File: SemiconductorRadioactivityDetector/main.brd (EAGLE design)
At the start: 32 parts, among them IC1 317T, IC3 LM324N, Q1 2N4093

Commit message: PCB done.
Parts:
- removed C11: 100n, resistor:C1206
- removed IC3: LM324N, linear:DIL14
- removed INTEGRATED_OUTPUT, LOGIC_LEVEL_OUTPUT, RAW_OUTPUT1: 22-05-7028-02, con-molex:7395-02
- removed R16: 10M, resistor:0204V
- added C10: 100n, resistor:C1206
- added IC2: 317T, linear:TO220H
- added J2, J3, J4: 22-23-2021, con-molex:22-23-2021
- added R8: 240R, resistor:M1206
- C1: value 15n -> 100n
- C6: value 100n -> 15n
- IC1: value 317T -> LM324N; device linear:TO220H -> linear:DIL14
- R1: value 240R -> 10M; device resistor:M1206 -> resistor:0204V
- R10: value 1M -> 4k7
- R11: value 100k -> 1k; device resistor:M1206 -> pot:B64Y
- R12: device resistor:M1206 -> resistor:R1206
- R13: value 1M -> 100k
- R14: value 47k -> 1M
- R2: value 2k -> 1M
- R3: value 1M -> 47k
- R5: value 100k -> 1M
- R7: value 1k -> 100k; device pot:B64Y -> resistor:M1206
- R9: value 4k7 -> 2k
- moved Q1 237.3 mm to (67.3, 14.0), flipped to the bottom
- moved D1 236.8 mm to (72.4, 15.2), flipped to the bottom
- moved C9 221.4 mm to (32.4, 6.35), flipped to the bottom, turned to 270 degrees
- moved R14 188.8 mm to (29.2, 6.35), flipped to the bottom, turned to 90 degrees
- moved C8 188.6 mm to (13.3, 10.2), flipped to the bottom
- moved R13 185.1 mm to (32.4, 12.1), flipped to the bottom, turned to 90 degrees
- moved C5 184.6 mm to (19.1, 14.6), flipped to the bottom, turned to 90 degrees
- moved C6 159.6 mm to (58.4, 19.1), flipped to the bottom, turned to 90 degrees
- moved R12 157.6 mm to (35.6, 12.1), flipped to the bottom, turned to 270 degrees
- moved R11 153.9 mm to (28.6, 17.8), turned to 90 degrees
- moved R10 141.7 mm to (25.4, 12.1), flipped to the bottom, turned to 90 degrees
- moved R7 133.3 mm to (50.2, 19.1), flipped to the bottom, turned to 270 degrees
- moved R6 126.4 mm to (54.6, 17.1), flipped to the bottom
- moved C1 121.7 mm to (71.1, 10.2), flipped to the bottom
- moved R9 112.5 mm to (10.8, 5.71), flipped to the bottom, turned to 270 degrees
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- renumbered POWER_SUPPLY to J1
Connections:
- net GND: now also C6.2, IC1.11, J2.2, J3.2, J4.1, R1.2, R11.A, R9.1; no longer C11.2, IC3.11, INTEGRATED_OUTPUT.2, LOGIC_LEVEL_OUTPUT.1, R16.2, R2.1, R7.A, RAW_OUTPUT1.2
- net N$1: now also IC2.1, R8.1, R9.2; no longer IC1.1, R1.1, R2.2
- net N$11: now also IC1.9, R11.S; no longer IC3.9, R7.S
- net N$12: now also C10.1, IC1.13, R13.1, R14.2; no longer C6.1, IC3.13, R10.2, R11.1
- net N$13: now also C10.2, IC1.14, J3.1, R14.1; no longer C6.2, IC3.14, INTEGRATED_OUTPUT.1, R10.1
- net N$14: now also IC1.12; no longer IC3.12
- net N$15: now also IC1.8, J4.2; no longer IC3.8, LOGIC_LEVEL_OUTPUT.2
- net N$16: now also C1.1, R2.2; no longer C5.1, R13.2
- net N$17: now also R1.1; no longer R16.1
- net N$18: now also IC1.3, R3.1; no longer IC3.3, R14.1
- net N$19: now also IC1.10, IC1.7, J2.1, R13.2, R7.1; no longer IC3.10, IC3.7, R11.2, R5.1, RAW_OUTPUT1.1
- net N$2: now also IC1.2, R5.2; no longer IC3.2, R3.2
- net N$3: now also IC1.1, IC1.5, R5.1; no longer IC3.1, IC3.5, R3.1
- net N$4: now also C4.1; no longer C1.1
- net N$5: now also IC1.6, R7.2; no longer IC3.6, R5.2
- net N$7: now also C6.1; no longer C4.1
- net N$8: now also C5.1, IC2.3; no longer C2.1, IC1.3
- net N$9: now also R10.2, R11.E; no longer R7.E, R9.2
- net VCC: now also C2.1, IC1.4, IC2.2, R10.1, R2.1, R3.2, R8.2; no longer C11.1, IC1.2, IC3.4, R1.2, R13.1, R14.2, R9.1
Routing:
- net VCC: track 8.44 -> 94.1 mm
- net N$19: track 0.00 -> 26.7 mm
- net N$18: track 0.00 -> 23.8 mm
- net N$3: track 0.00 -> 17.7 mm, vias 0 -> 2
- net N$13: track 0.00 -> 13.4 mm
- net N$12: track 0.00 -> 12.5 mm
- net N$11: track 0.00 -> 10.2 mm
- net N$17: track 0.00 -> 9.79 mm
- net N$5: track 0.00 -> 7.12 mm
- net N$2: track 0.00 -> 6.40 mm
- net N$16: track 0.00 -> 5.77 mm
- net N$9: track 0.00 -> 4.21 mm
- net N$15: track 0.00 -> 4.07 mm
- net N$14: track 0.00 -> 3.38 mm
- net N$4: track 0.00 -> 3.18 mm
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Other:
- board text added: "OUT INTEG."
- board text added: "OUT LOGIC."
- board text added: "OUT RAW"
- board text added: "POWER SUPPLY 14-16V DC"
- board text removed: "DC IN SUPPLY"
- board text removed: "HIGH VOLTAGE"
- board text removed: "HV OUT A"
- board text removed: "HV OUT B"

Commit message: Second version. Not working.
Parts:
- removed J2, J3, J4: 22-23-2021, con-molex:22-23-2021
- removed R14: 1M, resistor:M1206
- added C11: 10n, resistor:C0805
- added C12: 10n, rcl:C0805
- added C13: 100n, rcl:C0805
- added C14, C15: 100p, resistor:C0805
- added C16: 100n, resistor:C0805
- added IC3: OPA2333D, linear:SO08
- added PAD1, PAD2: (no value), wirepad:1,6/0,8
- added TP1, TP2, TP3, TP5: PTR1TP12R, testpad:TP12R
- C1, C5, C8: device resistor:C1206 -> rcl:C0805
- C10: value 100n -> 4p7; device resistor:C1206 -> resistor:C0805
- C2: value 100n -> 330n; device resistor:C1206 -> rcl:C0805
- C4: value 15n -> 330n; device resistor:C1206 -> rcl:C0805
- C6: value 15n -> 10n; device resistor:C1206 -> resistor:C0805
- C7: value 100n -> 10n; device resistor:C1206 -> resistor:C0805
- C9: value 100n -> 100p; device resistor:C1206 -> resistor:C0805
- IC1: value LM324N -> 78L08Z; device linear:DIL14 -> linear:TO92
- IC2: value 317T -> OPA2333D; device linear:TO220H -> linear:SO08
- R10: value 4k7 -> 1k; device resistor:M1206 -> rcl:R0805
- R11: device pot:B64Y -> rcl:R0805
- R12: value 100k -> 10k; device resistor:R1206 -> rcl:R0805
- R13: value 100k -> 10k; device resistor:M1206 -> rcl:R0805
- R2: value 1M -> 10k; device resistor:M1206 -> rcl:R0805
- R3: value 47k -> 10k; device resistor:M1206 -> rcl:R0805
- R4: value 1k -> 470k; device resistor:M1206 -> rcl:R0805
- R5: value 1M -> 39k; device resistor:M1206 -> rcl:R0805
- R6: value 1k -> 10R; device resistor:M1206 -> rcl:R0805
- R7: value 100k -> 1k; device resistor:M1206 -> rcl:R0805
- R8: value 240R -> 10k; device resistor:M1206 -> rcl:R0805
- R9: value 2k -> 10M; device resistor:M1206 -> rcl:0204V
- moved R2 68.9 mm to (5.08, 26.7)
- moved C1 68.9 mm to (3.17, 21.6)
- moved R3 63.0 mm to (5.08, 24.1), turned to 0 degrees
- moved C7 47.7 mm to (3.17, 10.2), turned to 90 degrees
- moved R7 45.0 mm to (5.71, 12.1)
- moved Q1 41.5 mm to (26.0, 10.2)
- moved D1 41.4 mm to (31.1, 12.1)
- moved R6 38.4 mm to (17.8, 6.35), turned to 180 degrees
- moved R1 38.3 mm to (26.7, 14.6)
- moved C6 38.0 mm to (21.6, 9.53), turned to 0 degrees
- moved C4 33.7 mm to (22.2, 5.71)
- moved C2 32.4 mm to (30.5, 6.99), turned to 0 degrees
- moved C9 31.4 mm to (3.17, 17.8)
- moved IC1 30.5 mm to (14.0, 23.5), turned to 0 degrees
- moved R13 29.9 mm to (3.17, 5.71), turned to 270 degrees
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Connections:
- removed net N$1: IC2.1, R8.1, R9.2
- removed net N$12: C10.1, C9.1, IC1.13, R13.1, R14.2
- removed net N$18: IC1.3, Q1.2, R3.1
- removed net N$19: IC1.10, IC1.7, J2.1, R13.2, R7.1
- removed net N$5: IC1.6, R6.2, R7.2
- removed net VCC: C2.1, C7.1, C8.1, IC1.4, IC2.2, R10.1, R2.1, R3.2, R8.2
- new net N$10: C9.1, IC2.2, R7.1, R8.2
- new net N$20: C10.2, C11.1, IC3.1, R9.1
- new net N$22: C12.1, C9.2, IC2.1, R8.1
- new net N$6: C6.1, Q1.2, R5.1
- new net V+: C13.1, C16.1, C4.1, C8.1, IC1.1, IC2.8, IC3.8, R2.2, R4.1, R5.2, TP3.TP
- new net V_REF: C1.1, IC2.3, IC2.5, IC3.3, IC3.5, R2.1, R3.2, TP1.TP
- net GND: now also C13.2, C16.2, IC1.2, IC2.4, IC3.4, PAD2.1, R3.1; no longer C6.2, C7.2, IC1.11, J2.2, J3.2, J4.1, R11.A, R12.1, R9.1
- net N$11: now also C7.2, R7.2; no longer IC1.9, R11.S
- net N$13: now also C14.1, IC2.6, R11.1, R12.2; no longer C10.2, C9.2, IC1.14, J3.1, R14.1
- net N$14: now also C12.2, R11.2; no longer IC1.12, R12.2
- net N$15: now also C11.2, R10.2; no longer IC1.8, J4.2
- net N$16: now also C2.1, R4.2; no longer C1.1, R2.2
- net N$2: now also C6.2, R6.2; no longer IC1.2, R4.2, R5.2
- net N$3: now also C14.2, IC2.7, PAD1.1, R12.1; no longer IC1.1, IC1.5, R5.1
- net N$4: now also C10.1, IC3.2, R6.1, R9.2; no longer C4.1, R4.1
- net N$7: now also C15.2, C7.1, IC3.7, R13.1, TP5.TP; no longer C6.1, R6.1
- net N$8: now also IC1.3, TP2.TP; no longer IC2.3
- net N$9: now also C15.1, IC3.6, R10.1, R13.2; no longer R10.2, R11.E
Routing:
- net VCC: track 94.1 -> 0.00 mm
- net V+: track 0.00 -> 76.5 mm, vias 0 -> 3
- net V_REF: track 0.00 -> 41.5 mm, vias 0 -> 2
- net N$19: track 26.7 -> 0.00 mm
- net N$18: track 23.8 -> 0.00 mm
- net N$10: track 0.00 -> 17.9 mm
- net N$12: track 12.5 -> 0.00 mm
- net N$22: track 0.00 -> 8.82 mm
- net N$1: track 8.31 -> 0.00 mm
- net N$9: track 4.21 -> 12.4 mm
- net N$7: track 2.73 -> 10.6 mm
- net N$11: track 10.2 -> 2.54 mm
- net N$20: track 0.00 -> 7.30 mm
- net N$3: track 17.7 -> 10.5 mm, vias 2 -> 0
- net N$5: track 7.12 -> 0.00 mm
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- added copper zone on layer 1, net GND
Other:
- board outline added: 34.9 x 32.4 mm
- board text added: "rev3.0"
- board text removed: "OUT INTEG."
- board text removed: "OUT LOGIC."
- board text removed: "OUT RAW"
- board text removed: "POWER SUPPLY 14-16V DC"
- board text removed: "rev2.0"

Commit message: Third HW revision, paritialy done.
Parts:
- removed C10: 4p7, resistor:C0805
- removed C11: 10n, resistor:C0805
- removed C12: 10n, rcl:C0805
- removed C13: 100n, rcl:C0805
- removed C14, C15, C9: 100p, resistor:C0805
- removed C16: 100n, resistor:C0805
- removed IC3: OPA2333D, linear:SO08
- removed J1: 22-05-7028-02, con-molex:7395-02
- removed PAD1, PAD2: (no value), wirepad:1,6/0,8
- removed Q1: 2N4093, transistor-fet:TO18
- removed R11: 1k, rcl:R0805
- removed R12, R13: 10k, rcl:R0805
- removed TP1, TP2, TP5: PTR1TP12R, testpad:TP12R
- added D2, D3: BPW32, opto-trans-siemens:BPW32
- added SL1: (no value), con-amp-quick:02P
- added U1: TPS7A470, regulator-jqi:S-PVQFN-N20
- added X1: LTI-SASF54GT, con-coax:LTI-SASF54GT
- C1, C5: value 100n -> 330n
- C2: value 330n -> (none); device rcl:C0805 -> resistor:T/3528-12R
- C3: value 100u/16V -> 100n; device rcl:153CLV-0505 -> rcl:C0805
- C6: value 10n -> 100n; device resistor:C0805 -> rcl:C0805
- C7: value 10n -> 330n; device resistor:C0805 -> rcl:C0805
- C8: value 100n -> 330n; device rcl:C0805 -> rcl:C1206K
- D1: value BP104 -> BPW32; device opto-trans-siemens:BP104 -> opto-trans-siemens:BPW32
- IC1: value 78L08Z -> LF356D; device linear:TO92 -> linear:SO08
- IC2: value OPA2333D -> LF356D
- R1: value 10M -> 10k; device resistor:0204V -> rcl:R1206
- R10, R7: value 1k -> 10k
- R3: value 10k -> (none); device rcl:R0805 -> resistor:MINI_MELF-0204W
- R4: value 470k -> (none); device rcl:R0805 -> resistor:MINI_MELF-0204W
- R5: value 39k -> (none); device rcl:R0805 -> resistor:RTRIM64W
- R6: value 10R -> (none); device rcl:R0805 -> resistor:M0805
- R8: value 10k -> (none); device rcl:R0805 -> resistor:M0805
- R9: value 10M -> (none); device rcl:0204V -> resistor:M0805
- moved R8 27.3 mm to (29.0, 3.57), turned to 180 degrees
- moved C7 25.6 mm to (28.8, 10.7), turned to 180 degrees
- moved D1 25.5 mm to (5.59, 11.2), flipped to the top, turned to 90 degrees
- moved R3 21.7 mm to (12.7, 3.81), turned to 270 degrees
- moved IC2 21.5 mm to (28.2, 7.11)
- moved C6 19.9 mm to (24.8, 29.2), turned to 180 degrees
- moved C8 19.3 mm to (19.2, 7.75), turned to 180 degrees
- moved R5 19.1 mm to (5.75, 4.00), turned to 180 degrees
- moved R7 18.7 mm to (24.4, 10.8), turned to 180 degrees
- moved TP3 18.2 mm to (22.2, 17.8)
- moved C5 17.1 mm to (14.0, 7.62)
- moved C2 17.1 mm to (29.3, 24.0), turned to 90 degrees
- moved R9 16.6 mm to (33.6, 9.06), flipped to the bottom, turned to 90 degrees
- moved R4 15.3 mm to (15.2, 3.81), turned to 90 degrees
- moved R10 12.5 mm to (22.9, 6.86)
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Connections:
- removed net N$11: C7.2, R7.2
- removed net N$13: C14.1, IC2.6, R11.1, R12.2
- removed net N$16: C2.1, D1.K, R4.2
- removed net N$17: D1.A, Q1.3, R1.1
- removed net N$20: C10.2, C11.1, IC3.1, R9.1
- removed net N$22: C12.1, C9.2, IC2.1, R8.1
- removed net V_REF: C1.1, IC2.3, IC2.5, IC3.3, IC3.5, R2.1, R3.2, TP1.TP
- new net N$1: C5.2, C8.1, IC1.6, R4.2
- new net N$5: C6.1, U1.14
- net GND: now also C2.-, C3.2, C6.2, C7.2, D1.A, D2.A, D3.A, IC1.4, R10.1, R2.1, R6.1, SL1.1, U1.10, U1.11, U1.12, U1.17, U1.18, U1.19, U1.2, U1.4, U1.5, U1.6, U1.7, U1.8, U1.9, U1.EXP, X1.2, X1.3, X1.4, X1.5; no longer C13.2, C16.2, C2.2, C3.-, C5.2, C8.2, IC1.2, IC3.4, J1.2, PAD2.1, Q1.1, R1.2, R3.1
- net N$10: now also C8.2, IC2.3, R10.2; no longer C9.1, IC2.2, R8.2
- net N$14: now also C1.1, IC1.3, R1.1, R2.2; no longer C12.2, R11.2
- net N$15: now also R9.2, X1.1; no longer C11.2, R10.2
- net N$2: now also IC2.2, R8.1; no longer C6.2
- net N$3: now also R3.2, R4.1; no longer C14.2, IC2.7, PAD1.1, R12.1
- net N$4: now also C5.1, D1.K, D2.K, D3.K, IC1.2, R3.1; no longer C10.1, IC3.2, R6.1, R9.2
- net N$6: now also IC1.1; no longer C6.1, Q1.2
- net N$7: now also IC1.5, R5.3; no longer C15.2, C7.1, IC3.7, R13.1, TP5.TP
- net N$8: now also C2.+, C3.1, SL1.2, U1.13, U1.15, U1.16; no longer C3.+, C5.1, IC1.3, J1.1, TP2.TP
- net N$9: now also IC2.6, R8.2, R9.1; no longer C15.1, IC3.6, R10.1, R13.2
- net V+: now also C7.1, IC1.7, IC2.7, R1.2, R7.2, U1.1, U1.20, U1.3; no longer C13.1, C16.1, C8.1, IC1.1, IC2.8, IC3.8, R2.2, R4.1
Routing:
- net V_REF: track 41.5 -> 0.00 mm, vias 2 -> 0
- net N$7: track 10.6 -> 27.7 mm, vias 0 -> 2
- net V+: track 76.5 -> 63.5 mm, vias 3 -> 0
- net N$13: track 11.8 -> 0.00 mm
- net N$1: track 0.00 -> 11.6 mm
- net N$10: track 17.9 -> 8.19 mm
- net N$22: track 8.82 -> 0.00 mm
- net N$14: track 2.54 -> 11.2 mm
- net N$15: track 2.54 -> 10.8 mm
- net N$17: track 8.04 -> 0.00 mm
- net N$3: track 10.5 -> 2.54 mm
- net N$4: track 9.06 -> 17.0 mm
- net N$20: track 7.30 -> 0.00 mm
- net N$8: track 12.6 -> 17.9 mm, vias 0 -> 2
- net N$16: track 5.21 -> 0.00 mm
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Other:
- board text added: "rev4.0"
- board text removed: "rev3.0"

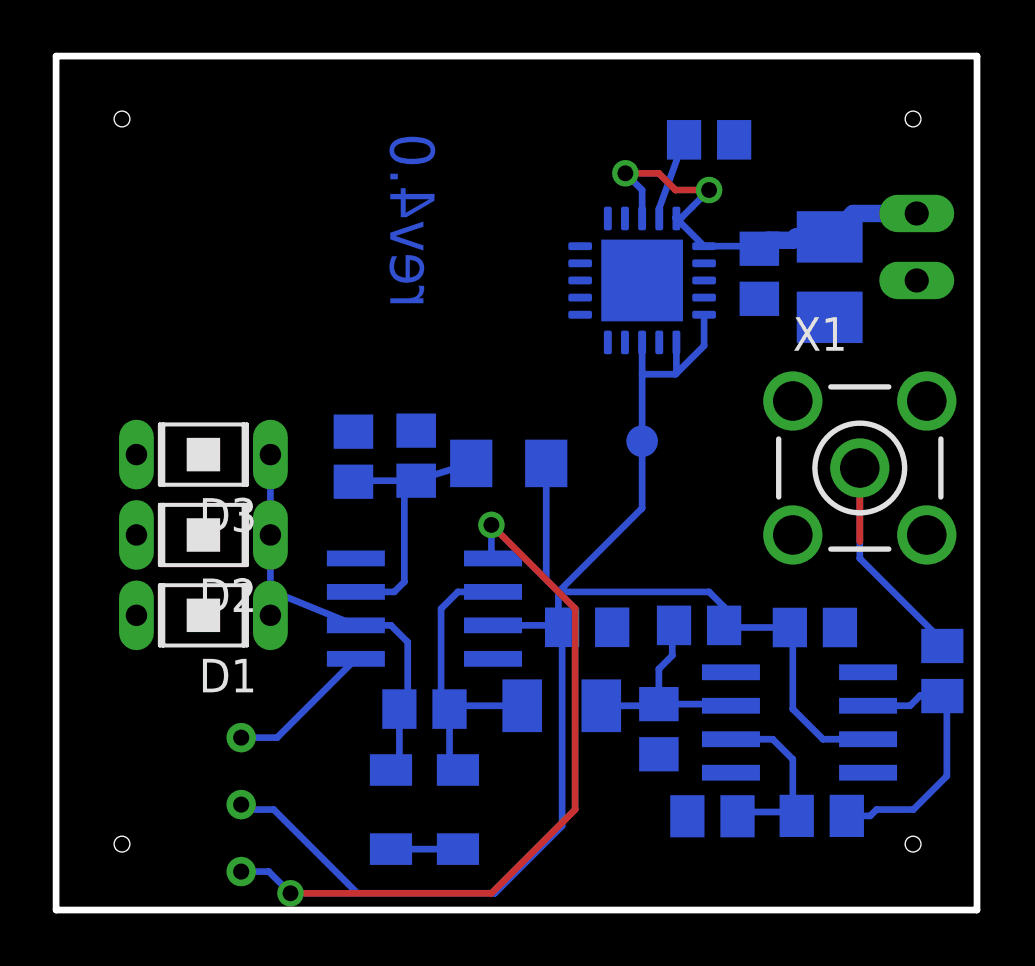
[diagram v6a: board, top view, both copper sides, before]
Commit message: Removed obsolete project, PCB fixes.
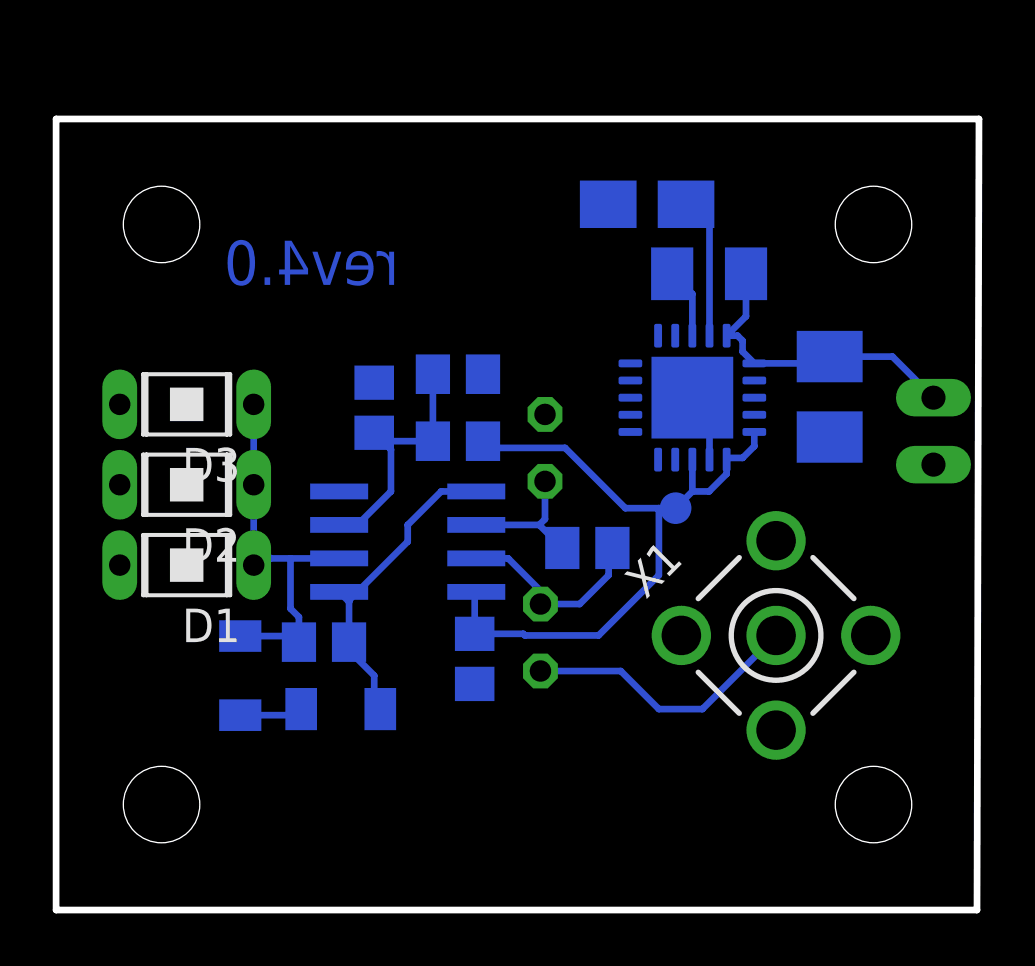
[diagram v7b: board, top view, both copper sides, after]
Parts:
- removed C4, C7: 330n, rcl:C0805
- removed C8: 330n, rcl:C1206K
- removed IC1, IC2: LF356D, linear:SO08
- removed R10, R7: 10k, rcl:R0805
- added IC3: NE5532D, linear:SO08
- C6: device rcl:C0805 -> rcl:A/3216-18W
- R1: device rcl:R1206 -> rcl:R0805
- R5: device resistor:RTRIM64W -> resistor:M1206
- R6, R9: device resistor:M0805 -> resistor:0204V
- moved R5 27.7 mm to (24.8, 24.1), turned to 0 degrees
- moved C3 18.2 mm to (15.9, 9.53)
- moved R6 15.3 mm to (18.5, 17.5), turned to 270 degrees
- moved R9 15.3 mm to (18.4, 10.3), turned to 270 degrees
- moved R8 13.5 mm to (20.1, 13.7)
- moved R3 7.65 mm to (6.99, 8.89)
- moved X1 7.10 mm to (27.3, 10.4), turned to 45 degrees
- moved SL1 7.01 mm to (33.3, 18.2)
- moved R4 5.85 mm to (10.8, 7.62), turned to 180 degrees
- moved R2 5.05 mm to (15.2, 20.3), turned to 0 degrees
- moved U1 4.84 mm to (24.1, 19.4)
- moved C5 4.58 mm to (10.2, 10.2)
- moved C2 4.54 mm to (29.3, 19.5)
- moved C6 3.39 mm to (22.4, 26.8)
- moved TP3 2.84 mm to (23.5, 15.2)
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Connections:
- removed net N$10: C8.2, IC2.3, R10.2, R7.1
- removed net N$7: IC1.5, R5.3
- net GND: now also C6.-, IC3.4; no longer C4.2, C6.2, C7.2, IC1.4, IC2.4, R10.1, U1.12, U1.6, U1.9
- net N$1: now also IC3.1, IC3.5; no longer C8.1, IC1.6
- net N$14: now also IC3.3; no longer IC1.3
- net N$2: now also IC3.6; no longer IC2.2
- net N$4: now also IC3.2; no longer IC1.2
- net N$5: now also C6.+; no longer C6.1
- net N$6: now also R5.2, U1.13; no longer IC1.1, R5.1
- net N$8: now also R5.1; no longer C3.1, U1.13
- net N$9: now also IC3.7; no longer IC2.6
- net V+: now also C3.1, IC3.8; no longer C4.1, C7.1, IC1.7, IC2.7, R5.2, R7.2
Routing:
- net V+: track 63.5 -> 26.5 mm
- net N$7: track 27.7 -> 0.00 mm, vias 2 -> 0
- net N$10: track 8.19 -> 0.00 mm
- net N$8: track 17.9 -> 11.9 mm, vias 2 -> 0
- net N$5: track 3.15 -> 6.33 mm
- net N$6: track 5.59 -> 2.67 mm
- net N$9: track 10.5 -> 7.61 mm
- net GND: track 0.00 -> 2.62 mm
- net N$4: track 17.0 -> 15.2 mm
- net N$2: track 7.03 -> 5.37 mm
- net N$14: track 11.2 -> 9.88 mm
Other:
- board size 34.9 x 32.4 mm -> 35 x 30 mm
